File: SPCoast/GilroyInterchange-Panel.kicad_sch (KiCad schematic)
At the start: 17 parts, among them U6023 0x22, U6024 0x23

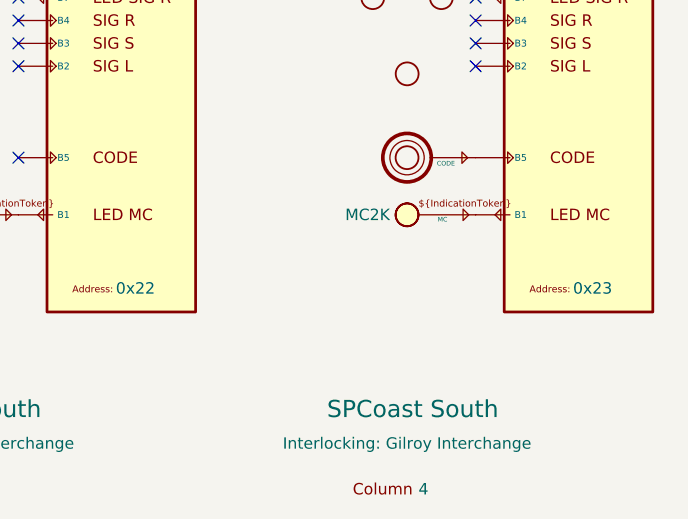
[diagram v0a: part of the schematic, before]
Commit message: chore(kicad): owner mockup: explicit seam wiring on Luchessa and South-cTc, host and bus pins
Owner's edits, committed as they stand (2026-10-21), before scripted edits build on them.

- Interlocking gains Codeline and Host pins; MAIN HOUSE's Interlocking pin is Codeline.
- OfficeUnit gains Host and Codeline pins; JohnCTC desk processor drawn on South-cTc.
- Processor gains Transport and IO pins; MAX7313 and MCP23017 gain an I2C bus pin.
- Transports: Codeline pin renamed Host; JMRI_MQTT instance added; Loconet removed.
- Encodings' pin renamed Transport; Luchessa's 506 and Bit Packing instances removed.
- SPCoastApp virtual host (FieldUnit_Virtual) hosts CMRInet and JMRI_MQTT.
- Luchessa: unit, houses and Time Coded on one net; Host to its own processor;
  panel MAX7313s on the desk bus (OfficeBus).
- Watsonville, Caltrain, Interchange: first-pass Processor placeholders, to be redrawn.

Verified: netlist and ERC exported from the saved project; field diff against the
committed netlist shows no per-instance field lost.
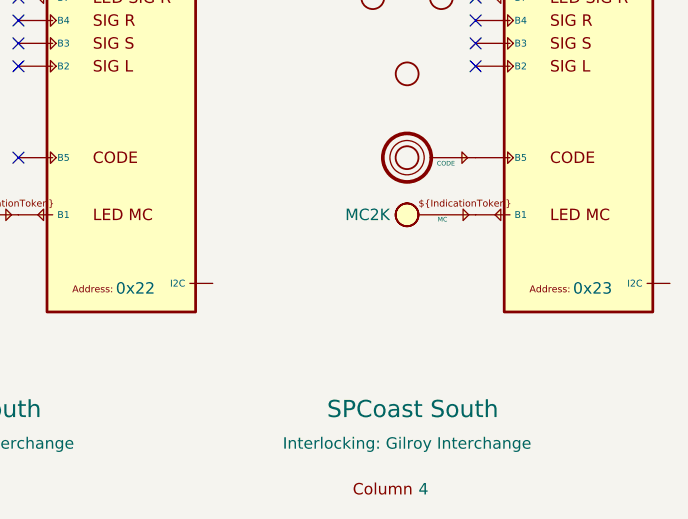
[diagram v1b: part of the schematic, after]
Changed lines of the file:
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@@
 		(pin "16"
+		)
+		(pin "17"
 		)
 		(instances
@@
 		(pin "16"
 		)
+		(pin "17"
+		)
 		(instances

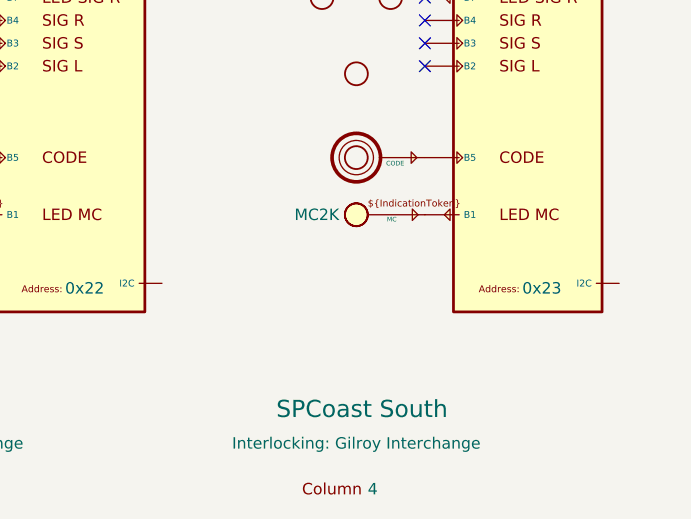
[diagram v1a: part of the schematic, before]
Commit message: chore(kicad): owner edits: uniform unit ports Codeline, Host, IOBus, OfficeIOBus; panels on the desk bus
Owner's edits, committed as they stand (2026-10-21): every unit sheet exposes the same four
ports and the parent wires only the ones it needs; Caltrain's and Interchange's panels reach
the desk bus through OfficeIOBus; unused ports carry no-connect flags; grid snaps fixed.
Two label spellings are still mismatched (Luchessa's OfficeIOBus vs the root's OfficeBusIO;
Interchange's JMRI_MQTT vs the root's IOBus), fixed in the next commit.
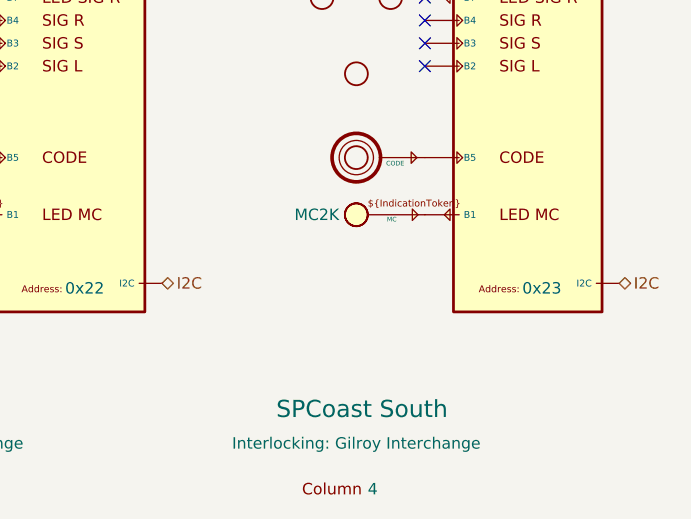
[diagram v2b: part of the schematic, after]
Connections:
- net I2C: now reaches U6024.17 (I2C)
- net I2C: now also U6023.17 (I2C)
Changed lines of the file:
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@@
 		(at 138.43 82.55)
+	)
+	(hierarchical_label "I2C"
+		(shape bidirectional)
+		(at 109.22 111.76 0)
+		(effects
+			(font
+				(size 1.27 1.27)
+			)
+			(justify left)
+		)
+	)
+	(hierarchical_label "I2C"
+		(shape bidirectional)
+		(at 160.02 111.76 0)
+		(effects
+			(font
+				(size 1.27 1.27)
+			)
+			(justify left)
+		)
 	)
 	(symbol

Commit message: chore(kicad): owner edits: Remote-IO node fields (Kind CMRI / MQTT-JMRI, bytes, UA), Interlocking Name, IOBus pins on remote drivers, sheet cleanup
Owner's edits of 2026-10-22, committed as they stand before the read-back.
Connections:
- net I2C renamed IOBus
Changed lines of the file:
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@@
 		(at 138.43 82.55)
 	)
-	(hierarchical_label "I2C"
+	(hierarchical_label "IOBus"
 		(shape bidirectional)
-		(at 109.22 111.76 0)
+		(at 111.76 111.76 0)
 		(effects
 			(font
@@
 		)
 	)
-	(hierarchical_label "I2C"
+	(hierarchical_label "IOBus"
 		(shape bidirectional)
-		(at 160.02 111.76 0)
+		(at 162.56 111.76 0)
 		(effects
 			(font
@@
 		(dnp no)
 		(property "Reference" "CDE6004"
-			(at 132.08 92.075 0)
+			(at 130.81 92.075 0)
 			(hide yes)
 			(show_name no)
@@
 		(dnp no)
 		(property "Reference" "LKL6004"
-			(at 130.81 71.12 0)
+			(at 130.81 65.405 0)
 			(hide yes)
 			(show_name no)
@@
 		(dnp no)
 		(property "Reference" "LKL6003"
-			(at 80.01 71.12 0)
+			(at 80.01 65.405 0)
 			(hide yes)
 			(show_name no)
@@
 		(dnp no)
 		(property "Reference" "LKL6003"
-			(at 80.01 71.12 0)
+			(at 80.01 65.405 0)
 			(hide yes)
 			(show_name no)
@@
 		(dnp no)
 		(property "Reference" "COL6024"
-			(at 130.81 133.985 0)
+			(at 125.73 120.65 0)
 			(hide yes)
 			(show_name no)
@@
 		(dnp no)
 		(property "Reference" "COL6023"
-			(at 80.01 133.985 0)
+			(at 74.93 120.65 0)
 			(hide yes)
 			(show_name no)
@@
 	(symbol
 		(lib_id "Railroad-HardwareIO:Driver-I2C-MAX7313-SPCoastcTc")
-		(at 149.86 72.39 0)
+		(at 151.13 72.39 0)
 		(unit 1)
 		(body_style 1)
@@
 		(dnp no)
 		(property "Reference" "U6024"
-			(at 142.24 22.86 0)
+			(at 143.51 22.86 0)
 			(hide yes)
 			(show_name no)
@@
 		)
 		(property "Value" "0x23"
-			(at 154.305 22.86 0)
+			(at 155.575 22.86 0)
 			(show_name no)
 			(do_not_autoplace yes)
@@
 		)
 		(property "Footprint" ""
-			(at 149.86 72.39 0)
+			(at 151.13 72.39 0)
 			(hide yes)
 			(show_name no)
@@
 		)
 		(property "Datasheet" ""
-			(at 149.86 72.39 0)
+			(at 151.13 72.39 0)
 			(hide yes)
 			(show_name no)
@@
 		)
 		(property "Description" "One physical IO expander instance bound to a PanelColumn. Address is 0x10 to 0x4F"
-			(at 163.195 17.78 0)
+			(at 164.465 17.78 0)
 			(hide yes)
 			(show_name no)
@@
 		)
 		(property "Role" "IODRIVER"
-			(at 148.59 107.315 0)
+			(at 149.86 107.315 0)
 			(hide yes)
 			(show_name no)
@@
 		)
 		(property "Address" "0x23"
-			(at 151.4281 112.3109 0)
+			(at 152.6981 112.3109 0)
 			(show_name no)
 			(do_not_autoplace no)
@@
 		)
 		(property "IC" "MAX7313"
-			(at 148.59 107.315 0)
+			(at 149.86 107.315 0)
 			(hide yes)
 			(show_name no)
@@
 		)
 		(property "Pin.A1" "binary"
-			(at 148.59 107.315 0)
+			(at 149.86 107.315 0)
 			(hide yes)
 			(show_name no)
@@
 		)
 		(property "Pin.A2" "binary"
-			(at 148.59 107.315 0)
+			(at 149.86 107.315 0)
 			(hide yes)
 			(show_name no)
@@
 		)
 		(property "Pin.A3" "binary"
-			(at 148.59 107.315 0)
+			(at 149.86 107.315 0)
 			(hide yes)
 			(show_name no)
@@
 		)
 		(property "Pin.A4" "binary"
-			(at 148.59 107.315 0)
+			(at 149.86 107.315 0)
 			(hide yes)
 			(show_name no)
@@
 		)
 		(property "Pin.A5" "binary"
-			(at 148.59 107.315 0)
+			(at 149.86 107.315 0)
 			(hide yes)
 			(show_name no)
@@
 		)
 		(property "Pin.A6" "binary"
-			(at 148.59 107.315 0)
+			(at 149.86 107.315 0)
 			(hide yes)
 			(show_name no)
@@
 		)
 		(property "Pin.A7" "binary"
-			(at 148.59 107.315 0)
+			(at 149.86 107.315 0)
 			(hide yes)
 			(show_name no)
@@
 		)
 		(property "Pin.A8" "binary"
-			(at 148.59 107.315 0)
+			(at 149.86 107.315 0)
 			(hide yes)
 			(show_name no)
@@
 		)
 		(property "Pin.B1" "binary"
-			(at 148.59 107.315 0)
+			(at 149.86 107.315 0)
 			(hide yes)
 			(show_name no)
@@
 		)
 		(property "Pin.B2" "binary"
-			(at 148.59 107.315 0)
+			(at 149.86 107.315 0)
 			(hide yes)
 			(show_name no)
@@
 		)
 		(property "Pin.B3" "binary"
-			(at 148.59 107.315 0)
+			(at 149.86 107.315 0)
 			(hide yes)
 			(show_name no)
@@
 		)
 		(property "Pin.B4" "binary"
-			(at 148.59 107.315 0)
+			(at 149.86 107.315 0)
 			(hide yes)
 			(show_name no)
@@
 		)
 		(property "Pin.B5" "binary"
-			(at 148.59 107.315 0)
+			(at 149.86 107.315 0)
 			(hide yes)
 			(show_name no)
@@
 		)
 		(property "Pin.B6" "binary"
-			(at 148.59 107.315 0)
+			(at 149.86 107.315 0)
 			(hide yes)
 			(show_name no)
@@
 		)
 		(property "Pin.B7" "binary"
-			(at 148.59 107.315 0)
+			(at 149.86 107.315 0)
 			(hide yes)
 			(show_name no)
@@
 		)
 		(property "Pin.B8" "binary"
-			(at 148.59 107.315 0)
+			(at 149.86 107.315 0)
 			(hide yes)
 			(show_name no)
@@
 	(symbol
 		(lib_id "Railroad-HardwareIO:Driver-I2C-MAX7313-SPCoastcTc")
-		(at 99.06 72.39 0)
+		(at 100.33 72.39 0)
 		(unit 1)
 		(body_style 1)
@@
 		(dnp no)
 		(property "Reference" "U6023"
-			(at 91.44 22.86 0)
+			(at 92.71 22.86 0)
 			(hide yes)
 			(show_name no)
@@
 		)
 		(property "Value" "0x22"
-			(at 103.505 22.86 0)
+			(at 104.775 22.86 0)
 			(show_name no)
 			(do_not_autoplace yes)
@@
 		)
 		(property "Footprint" ""
-			(at 99.06 72.39 0)
+			(at 100.33 72.39 0)
 			(hide yes)
 			(show_name no)
@@
 		)
 		(property "Datasheet" ""
-			(at 99.06 72.39 0)
+			(at 100.33 72.39 0)
 			(hide yes)
 			(show_name no)
@@
 		)
 		(property "Description" "One physical IO expander instance bound to a PanelColumn. Address is 0x10 to 0x4F"
-			(at 112.395 17.78 0)
+			(at 113.665 17.78 0)
 			(hide yes)
 			(show_name no)
@@
 		)
 		(property "Role" "IODRIVER"
-			(at 97.79 107.315 0)
+			(at 99.06 107.315 0)
 			(hide yes)
 			(show_name no)
@@
 		)
 		(property "Address" "0x22"
-			(at 100.6281 112.3109 0)
+			(at 101.8981 112.3109 0)
 			(show_name no)
 			(do_not_autoplace no)
@@
 		)
 		(property "IC" "MAX7313"
-			(at 97.79 107.315 0)
+			(at 99.06 107.315 0)
 			(hide yes)
 			(show_name no)
@@
 		)
 		(property "Pin.A1" "binary"
-			(at 97.79 107.315 0)
+			(at 99.06 107.315 0)
 			(hide yes)
 			(show_name no)
@@
 		)
 		(property "Pin.A2" "binary"
-			(at 97.79 107.315 0)
+			(at 99.06 107.315 0)
 			(hide yes)
 			(show_name no)
@@
 		)
 		(property "Pin.A3" "binary"
-			(at 97.79 107.315 0)
+			(at 99.06 107.315 0)
 			(hide yes)
 			(show_name no)
@@
 		)
 		(property "Pin.A4" "binary"
-			(at 97.79 107.315 0)
+			(at 99.06 107.315 0)
 			(hide yes)
 			(show_name no)
@@
 		)
 		(property "Pin.A5" "binary"
-			(at 97.79 107.315 0)
+			(at 99.06 107.315 0)
 			(hide yes)
 			(show_name no)
@@
 		)
 		(property "Pin.A6" "binary"
-			(at 97.79 107.315 0)
+			(at 99.06 107.315 0)
 			(hide yes)
 			(show_name no)
@@
 		)
 		(property "Pin.A7" "binary"
-			(at 97.79 107.315 0)
+			(at 99.06 107.315 0)
 			(hide yes)
 			(show_name no)
@@
 		)
 		(property "Pin.A8" "binary"
-			(at 97.79 107.315 0)
+			(at 99.06 107.315 0)
 			(hide yes)
 			(show_name no)
@@
 		)
 		(property "Pin.B1" "binary"
-			(at 97.79 107.315 0)
+			(at 99.06 107.315 0)
 			(hide yes)
 			(show_name no)
@@
 		)
 		(property "Pin.B2" "binary"
-			(at 97.79 107.315 0)
+			(at 99.06 107.315 0)
 			(hide yes)
 			(show_name no)
@@
 		)
 		(property "Pin.B3" "binary"
-			(at 97.79 107.315 0)
+			(at 99.06 107.315 0)
 			(hide yes)
 			(show_name no)
@@
 		)
 		(property "Pin.B4" "binary"
-			(at 97.79 107.315 0)
+			(at 99.06 107.315 0)
 			(hide yes)
 			(show_name no)
@@
 		)
 		(property "Pin.B5" "binary"
-			(at 97.79 107.315 0)
+			(at 99.06 107.315 0)
 			(hide yes)
 			(show_name no)
@@
 		)
 		(property "Pin.B6" "binary"
-			(at 97.79 107.315 0)
+			(at 99.06 107.315 0)
 			(hide yes)
 			(show_name no)
@@
 		)
 		(property "Pin.B7" "binary"
-			(at 97.79 107.315 0)
+			(at 99.06 107.315 0)
 			(hide yes)
 			(show_name no)
@@
 		)
 		(property "Pin.B8" "binary"
-			(at 97.79 107.315 0)
+			(at 99.06 107.315 0)
 			(hide yes)
 			(show_name no)
@@
 		(dnp no)
 		(property "Reference" "LKL6004"
-			(at 130.81 71.12 0)
-			(hide yes)
-			(show_name no)
+			(at 130.81 65.405 0)
+			(hide yes)
+			(show_name no)
